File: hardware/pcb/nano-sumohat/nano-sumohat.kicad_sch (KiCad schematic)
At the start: 10 parts, among them J1 Analog, J10 H-OUT, J2 Digital, J4 MH-8 IR Sensor Back, J5 MH-8 IR Sensor Front, J6 HC-SR04 Ultrasound, J7 H bridge, J8 IR Sensor Start, J9 BAT-IN, SW1 Power SW

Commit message: Add v1.1 for nano sumohat
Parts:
- removed J8: IR Sensor Start, Connector_PinSocket_2.54mm:PinSocket_1x03_P2.54mm_Vertical, symbol Connector_Generic:Conn_01x03
- added J3: IR Sensor Start, Connector_PinHeader_2.54mm:PinHeader_1x04_P2.54mm_Vertical, symbol Connector_Generic:Conn_01x04
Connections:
- net *D10/SS: no longer J6.2 (Pin_2)
- net *D11/MOSI: now also J6.3 (Pin_3)
- net *D3: now also J3.4 (Pin_4); no longer J7.4 (Pin_4)
- net *D5: now also J7.3 (Pin_3); no longer J7.2 (Pin_2)
- net *D6: now also J7.2 (Pin_2); no longer J7.1 (Pin_1)
- net *D9: now also J5.3 (Pin_3); no longer J6.3 (Pin_3)
- net +5V: now also J3.1 (Pin_1)
- net D12/MISO: now also J6.2 (Pin_2)
- net D2: now also J3.3 (Pin_3)
- net D4: now also J7.4 (Pin_4); no longer J7.3 (Pin_3)
- net D7: now also J7.1 (Pin_1); no longer J4.3 (Pin_3)
- net D8: now also J4.3 (Pin_3); no longer J5.3 (Pin_3)
- net GND: now also J3.2 (Pin_2)

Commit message: Add v2-draft6 build guide
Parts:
- added H1, H2, H3, H4: MountingHole, MountingHole:MountingHole_2.7mm_M2.5_DIN965_Pad_TopBottom, symbol Mechanical:MountingHole_Pad
- added J8: Extension, Connector_PinHeader_2.54mm:PinHeader_2x05_P2.54mm_Vertical, symbol Connector_Generic:Conn_02x05_Top_Bottom
- added SW2: ~, Button_Switch_THT:SW_Slide-03_Wuerth-WS-SLTV_10x2.5x6.4_P2.54mm, symbol Switch:SW_Wuerth_450301014042
- J3: value IR Sensor Start -> IR_START
- J4: value MH-8 IR Sensor Back -> IR_B
- J5: value MH-8 IR Sensor Front -> IR_F
- J6: value HC-SR04 Ultrasound -> SND_Sensor
- J7: value H bridge -> Motor; footprint Connector_PinHeader_2.54mm:PinHeader_1x04_P2.54mm_Vertical -> Connector_PinHeader_2.54mm:PinHeader_1x06_P2.54mm_Vertical; symbol Connector_Generic:Conn_01x04 -> Connector_Generic:Conn_01x06
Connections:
- net *D10/SS: now also J8.9 (Pin_9)
- net *D5: now also J7.4 (Pin_4); no longer J7.3 (Pin_3)
- net *D6: now also J7.3 (Pin_3); no longer J7.2 (Pin_2)
- net +5V: now also SW2.3 (A)
- net A0: now also J8.3 (Pin_3)
- net A1: now also J8.4 (Pin_4)
- net A2: now also J8.5 (Pin_5)
- net A3: now also J8.6 (Pin_6)
- net A4/SDA: now also J8.7 (Pin_7)
- net A5/SCL: now also J8.8 (Pin_8)
- net A6: now also J7.1 (Pin_1)
- net A7: now also J7.6 (Pin_6)
- net D0/RX: now also J8.1 (Pin_1)
- net D13/SCK: now also J8.10 (Pin_10)
- net D1/TX: now also J8.2 (Pin_2)
- net D2: now also SW2.1 (B); no longer J3.3 (Pin_3)
- net D4: now also J7.5 (Pin_5); no longer J7.4 (Pin_4)
- net D7: now also J7.2 (Pin_2); no longer J7.1 (Pin_1)
- net GND: now also H1.1, H2.1, H3.1, H4.1
- new net START: J3.3 (Pin_3), SW2.2 (C)
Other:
- note added: "Select either start signal or bypass"
- moved on the sheet: J10, J3, J4, J5, J6, J9, SW1

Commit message: Update PCB v1.2
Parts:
- removed SW1: Power SW, Button_Switch_THT:SW_E-Switch_EG1271_SPDT, symbol Switch:SW_DPST
- added SW1: ~, Button_Switch_THT:SW_Slide-03_Wuerth-WS-SLTV_10x2.5x6.4_P2.54mm, symbol Switch:SW_Wuerth_450301014042
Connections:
- net BAT_GND is gone; now on net GND: J9.1 (Pin_1)
- net BAT_VCC: now also SW1.1 (B)
- net VCC: now also SW1.3 (A)
- no-connect marks 0 -> 1
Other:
- moved on the sheet: J9
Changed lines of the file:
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@@
 	)
 	(junction
-		(at 146.05 40.64)
-		(diameter 0)
-		(color 0 0 0 0)
-	)
-	(junction
 		(at 262.89 154.94)
 		(diameter 0)
 		(color 0 0 0 0)
 	)
+	(no_connect
+		(at 154.94 39.37)
+	)
 	(wire
 		(pts
@@
 	(wire
 		(pts
-			(xy 138.43 53.34) (xy 146.05 53.34)
+			(xy 139.7 53.34) (xy 147.32 53.34)
 		)
 		(stroke
@@
 	(wire
 		(pts
-			(xy 146.05 40.64) (xy 146.05 41.91)
-		)
-		(stroke
-			(width 0)
-			(type default)
-		)
-	)
-	(wire
-		(pts
 			(xy 55.88 52.07) (xy 71.12 52.07)
 		)
@@
 	(wire
 		(pts
+			(xy 144.78 46.99) (xy 152.4 46.99)
+		)
+		(stroke
+			(width 0)
+			(type default)
+		)
+	)
+	(wire
+		(pts
 			(xy 17.78 34.29) (xy 35.56 34.29)
 		)
@@
 	(wire
 		(pts
-			(xy 138.43 55.88) (xy 146.05 55.88)
+			(xy 139.7 55.88) (xy 147.32 55.88)
 		)
 		(stroke
@@
 		(exclude_from_sim no)
 		(at 113.792 65.532 0)
-		(size 41.148 37.592)
+		(size 51.054 37.592)
 		(stroke
 			(width 0)
@@
 	)
 	(label "BAT_GND"
-		(at 138.43 55.88 0)
+		(at 139.7 55.88 0)
 		(fields_autoplaced yes)
 		(effects
@@
 	)
 	(label "BAT_VCC"
-		(at 138.43 53.34 0)
+		(at 139.7 53.34 0)
 		(fields_autoplaced yes)
 		(effects
@@
 		)
 	)
-	(label "BAT_GND"
-		(at 151.13 40.64 270)
-		(fields_autoplaced yes)
-		(effects
-			(font
-				(size 1.27 1.27)
-			)
-			(justify right bottom)
-		)
-	)
 	(label "*D9"
 		(at 71.12 34.29 180)
@@
 	)
 	(label "BAT_VCC"
-		(at 146.05 30.48 90)
+		(at 144.78 36.83 180)
 		(fields_autoplaced yes)
 		(effects
@@
 				(size 1.27 1.27)
 			)
-			(justify left bottom)
+			(justify right bottom)
 		)
 	)
@@
 		)
 	)
+	(label "BAT_GND"
+		(at 144.78 46.99 180)
+		(fields_autoplaced yes)
+		(effects
+			(font
+				(size 1.27 1.27)
+			)
+			(justify right bottom)
+		)
+	)
 	(label "D0{slash}RX"
 		(at 25.4 111.76 180)
@@
 	(symbol
 		(lib_id "power:VCC")
-		(at 151.13 30.48 0)
+		(at 154.94 34.29 270)
 		(unit 1)
 		(exclude_from_sim no)
@@
 		)
 		(property "Value" "VCC"
-			(at 151.13 26.67 90)
+			(at 158.75 34.29 90)
 			(effects
 				(font
@@
 		)
 		(property "Footprint" ""
-			(at 151.13 30.48 0)
+			(at 154.94 34.29 0)
 			(effects
 				(font
@@
 		)
 		(property "Datasheet" ""
-			(at 151.13 30.48 0)
+			(at 154.94 34.29 0)
 			(effects
 				(font
@@
 		)
 		(property "Description" ""
-			(at 151.13 30.48 0)
+			(at 154.94 34.29 0)
 			(effects
 				(font
@@
 	)
 	(symbol
+		(lib_id "power:GND")
+		(at 152.4 46.99 90)
+		(unit 1)
+		(exclude_from_sim no)
+		(in_bom yes)
+		(on_board yes)
+		(dnp no)
+		(property "Reference" "#PWR08"
+			(at 158.75 46.99 0)
+			(effects
+				(font
+					(size 1.27 1.27)
+				)
+				(hide yes)
+			)
+		)
+		(property "Value" "GND"
+			(at 156.21 46.99 0)
+			(effects
+				(font
+					(size 1.27 1.27)
+				)
+			)
+		)
+		(property "Footprint" ""
+			(at 152.4 46.99 0)
+			(effects
+				(font
+					(size 1.27 1.27)
+				)
+				(hide yes)
+			)
+		)
+		(property "Datasheet" ""
+			(at 152.4 46.99 0)
+			(effects
+				(font
+					(size 1.27 1.27)
+				)
+				(hide yes)
+			)
+		)
+		(property "Description" ""
+			(at 152.4 46.99 0)
+			(effects
+				(font
+					(size 1.27 1.27)
+				)
+				(hide yes)
+			)
+		)
+		(pin "1"
+		)
+		(instances
+			(project "nano-sumohat"
+				(path "/0d35483a-0b12-46cc-b9f2-896fd6831779"
+					(reference "#PWR08")
+					(unit 1)
+				)
+			)
+		)
+	)
+	(symbol
 		(lib_id "Switch:SW_Wuerth_450301014042")
 		(at 132.08 92.71 0)
@@
 	)
 	(symbol
-		(lib_id "Switch:SW_DPST")
-		(at 143.51 35.56 90)
-		(unit 1)
-		(exclude_from_sim no)
-		(in_bom yes)
-		(on_board yes)
-		(dnp no)
-		(fields_autoplaced yes)
-		(property "Reference" "SW1"
-			(at 152.4 34.925 90)
-			(effects
-				(font
-					(size 1.27 1.27)
-				)
-				(justify right)
-			)
-		)
-		(property "Value" "Power SW"
-			(at 152.4 37.465 90)
-			(effects
-				(font
-					(size 1.27 1.27)
-				)
-				(justify right)
-			)
-		)
-		(property "Footprint" "Button_Switch_THT:SW_E-Switch_EG1271_SPDT"
-			(at 132.08 31.75 0)
-			(effects
-				(font
-					(size 1.27 1.27)
-				)
-				(hide yes)
-			)
-		)
-		(property "Datasheet" "~"
-			(at 143.51 35.56 0)
-			(effects
-				(font
-					(size 1.27 1.27)
-				)
-				(hide yes)
-			)
-		)
-		(property "Description" ""
-			(at 143.51 35.56 0)
-			(effects
-				(font
-					(size 1.27 1.27)
-				)
-				(hide yes)
-			)
-		)
-		(pin "1"
-		)
-		(pin "2"
-		)
-		(pin "3"
-		)
-		(pin "4"
-		)
-		(pin "5"
-		)
-		(pin "6"
-		)
-		(instances
-			(project "nano-sumohat"
-				(path "/0d35483a-0b12-46cc-b9f2-896fd6831779"
-					(reference "SW1")
-					(unit 1)
-				)
-			)
-		)
-	)
-	(symbol
 		(lib_id "Connector_Generic:Conn_01x03")
 		(at 31.75 95.25 0)
@@
 	)
 	(symbol
-		(lib_id "power:GND")
-		(at 146.05 40.64 0)
+		(lib_id "Switch:SW_Wuerth_450301014042")
+		(at 149.86 36.83 0)
 		(unit 1)
 		(exclude_from_sim no)
@@
 		(on_board yes)
 		(dnp no)
-		(property "Reference" "#PWR012"
-			(at 146.05 46.99 0)
+		(property "Reference" "SW1"
+			(at 149.86 30.226 0)
 			(effects
 				(font
 					(size 1.27 1.27)
 				)
-				(hide yes)
 			)
 		)
-		(property "Value" "GND"
-			(at 146.05 44.45 0)
+		(property "Value" "~"
+			(at 149.86 31.75 0)
 			(effects
 				(font
@@
 			)
 		)
-		(property "Footprint" ""
-			(at 146.05 40.64 0)
+		(property "Footprint" "Button_Switch_THT:SW_Slide-03_Wuerth-WS-SLTV_10x2.5x6.4_P2.54mm"
+			(at 149.86 46.99 0)
 			(effects
 				(font
@@
 			)
 		)
-		(property "Datasheet" ""
-			(at 146.05 40.64 0)
+		(property "Datasheet" "https://www.we-online.com/components/products/datasheet/450301014042.pdf"
+			(at 149.86 44.45 0)
 			(effects
 				(font
@@
 			)
 		)
-		(property "Description" ""
-			(at 146.05 40.64 0)
+		(property "Description" "Switch slide, single pole double throw"
+			(at 149.86 36.83 0)
 			(effects
 				(font
@@
 			)
 		)
+		(pin "2"
+		)
+		(pin "3"
+		)
 		(pin "1"
 		)
@@
 			(project "nano-sumohat"
 				(path "/0d35483a-0b12-46cc-b9f2-896fd6831779"
-					(reference "#PWR012")
+					(reference "SW1")
 					(unit 1)
 				)
@@
 	(symbol
 		(lib_id "Connector:Conn_01x02_Pin")
-		(at 151.13 55.88 180)
+		(at 152.4 55.88 180)
 		(unit 1)
 		(exclude_from_sim no)
@@
 		(fields_autoplaced yes)
 		(property "Reference" "J9"
-			(at 152.4 53.975 0)
+			(at 153.67 53.975 0)
 			(effects
 				(font
@@
 		)
 		(property "Value" "BAT-IN"
-			(at 152.4 56.515 0)
+			(at 153.67 56.515 0)
 			(effects
 				(font
@@
 		)
 		(property "Footprint" "Connector_JST:JST_EH_B2B-EH-A_1x02_P2.50mm_Vertical"
-			(at 151.13 55.88 0)
+			(at 152.4 55.88 0)
 			(effects
 				(font
@@
 		)
 		(property "Datasheet" "~"
-			(at 151.13 55.88 0)
+			(at 152.4 55.88 0)
 			(effects
 				(font
@@
 		)
 		(property "Description" ""
-			(at 151.13 55.88 0)
+			(at 152.4 55.88 0)
 			(effects
 				(font

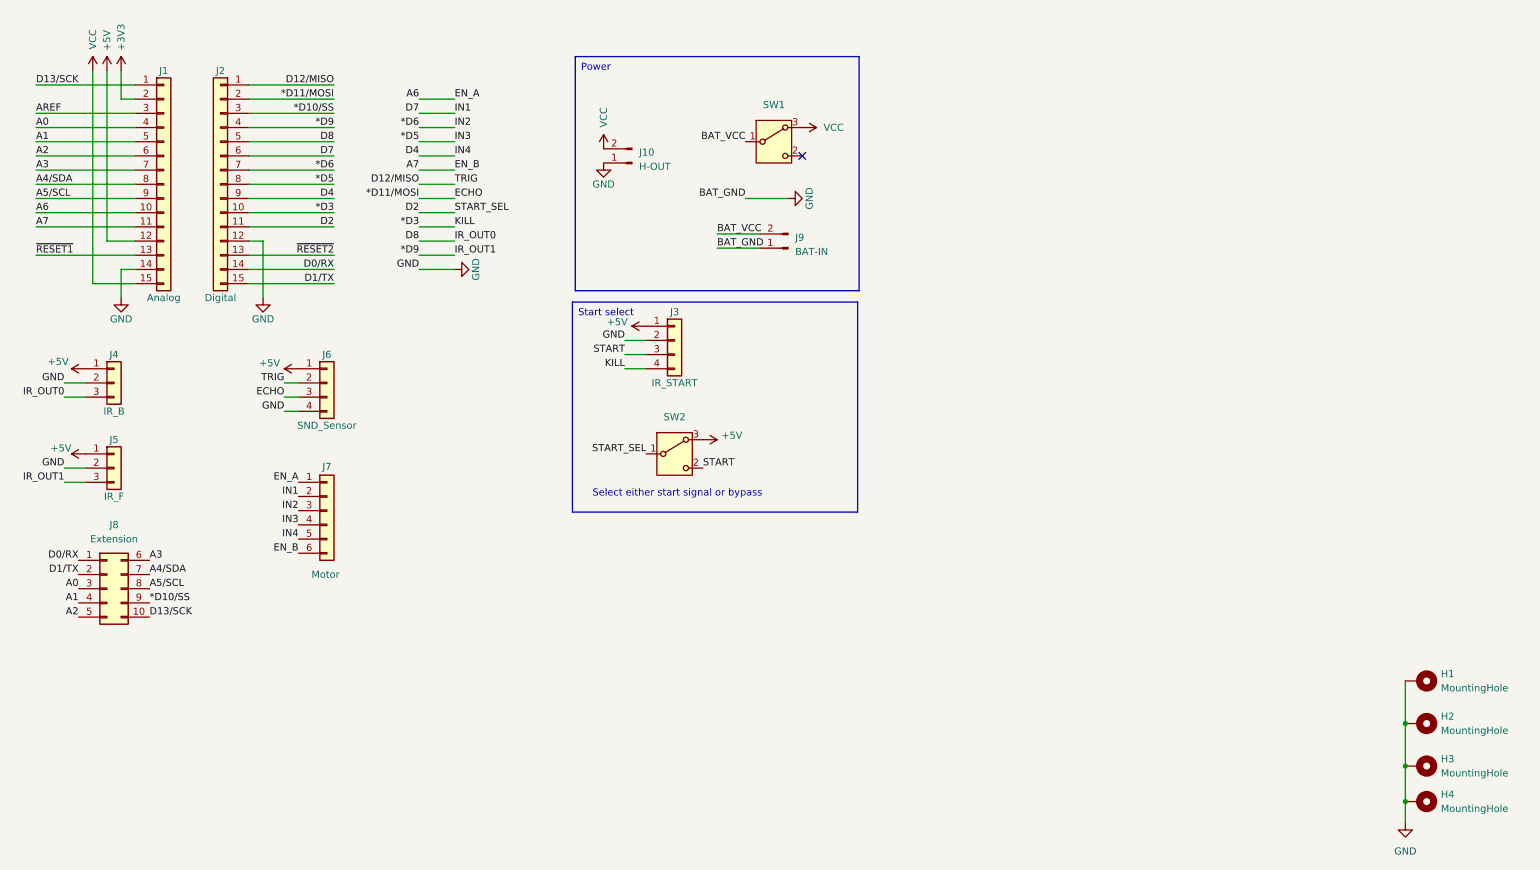
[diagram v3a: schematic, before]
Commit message: Update schematics with more comments
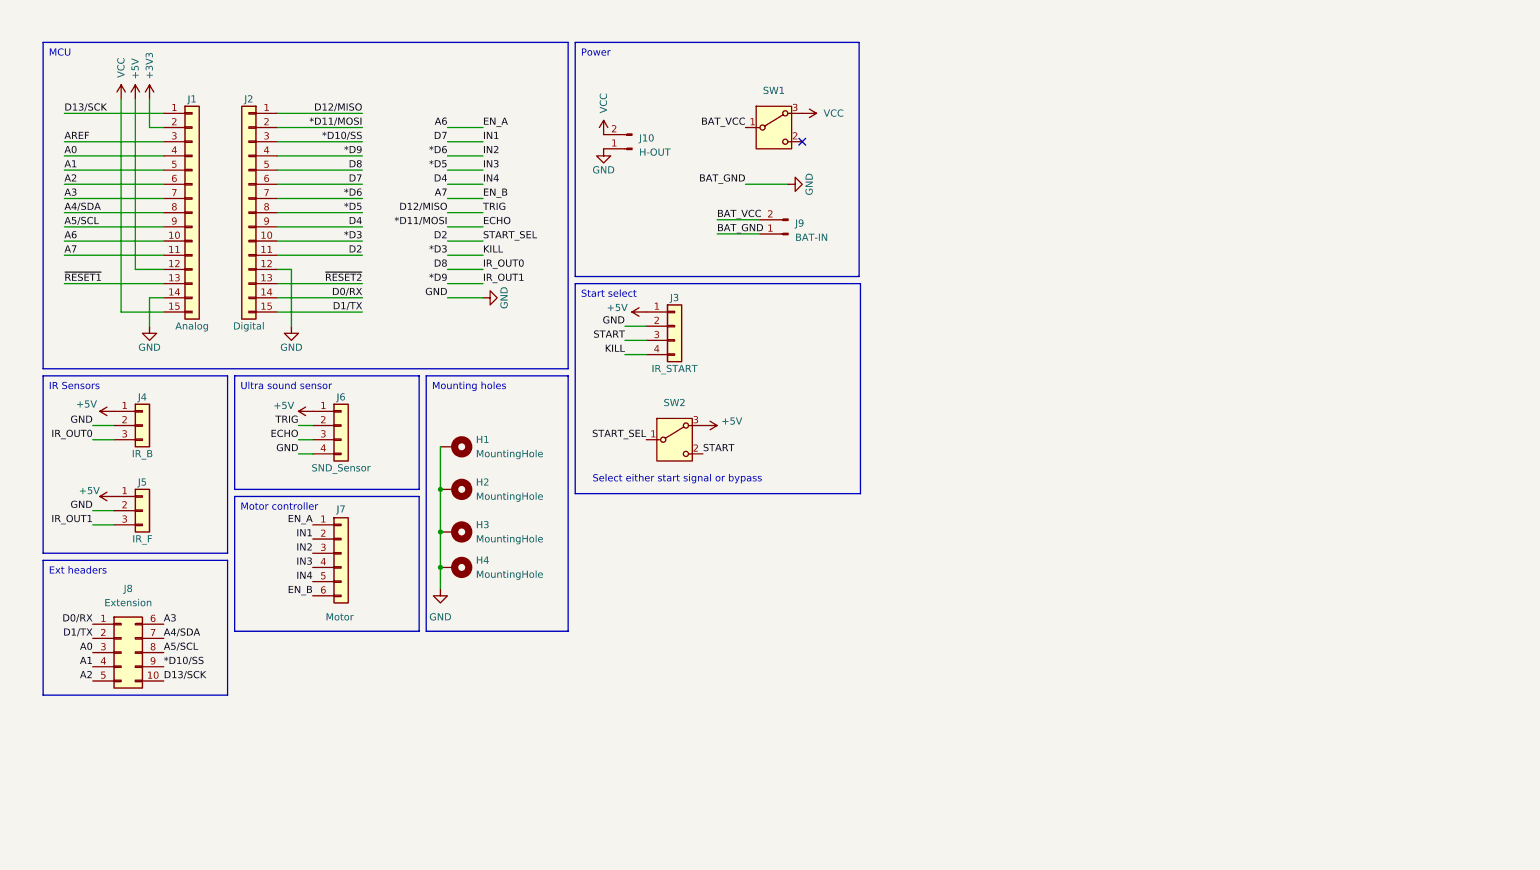
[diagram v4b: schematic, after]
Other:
- company: (none) -> K. Strålman
- title: (none) -> Nano sumohat
- moved on the sheet: H1, H2, H3, H4, J1, J10, J2, J3, J4, J5, J6, J7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
